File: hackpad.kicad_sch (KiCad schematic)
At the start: 1 part, among them U1 XIAO-RP2040-DIP

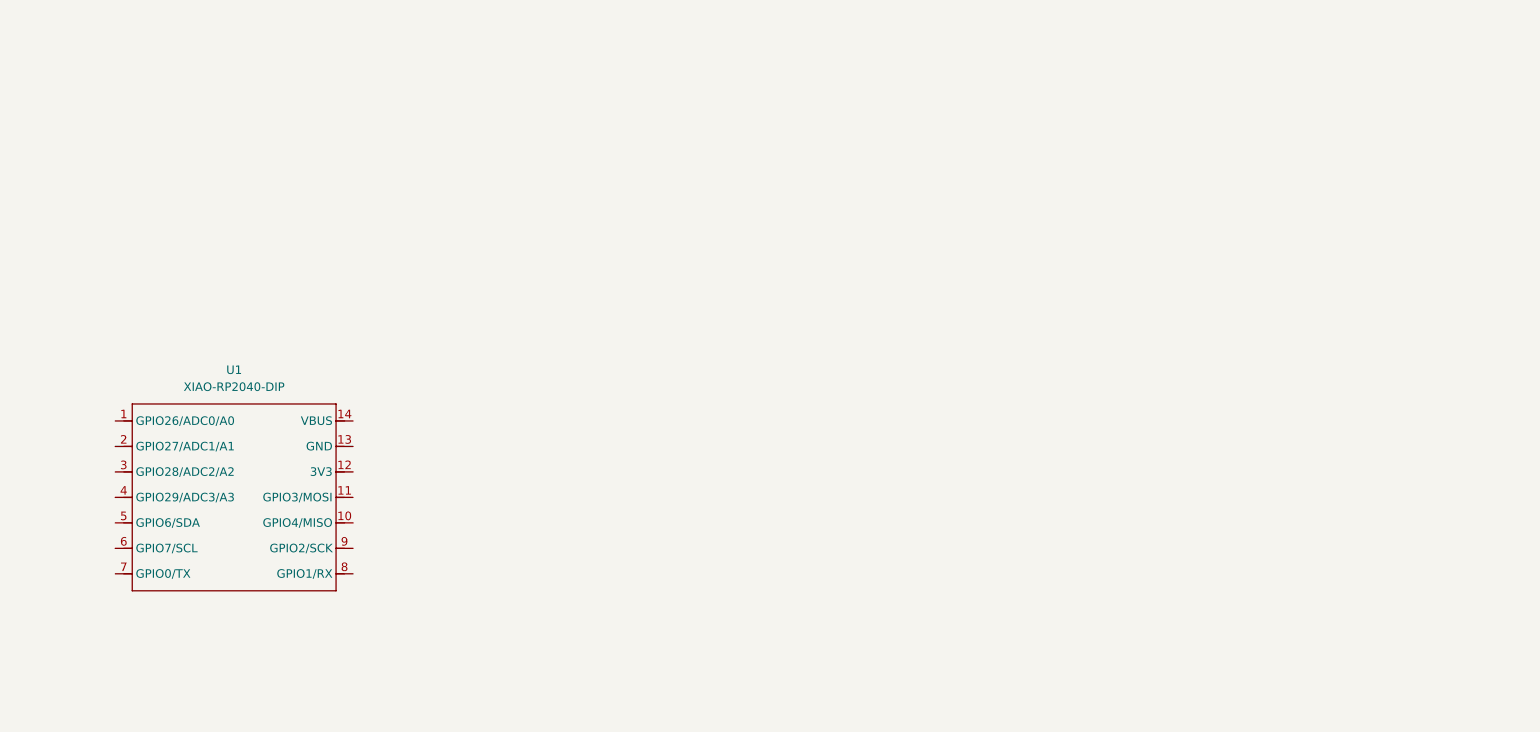
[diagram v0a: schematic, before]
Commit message: add keys, oled, neopixels to schematic
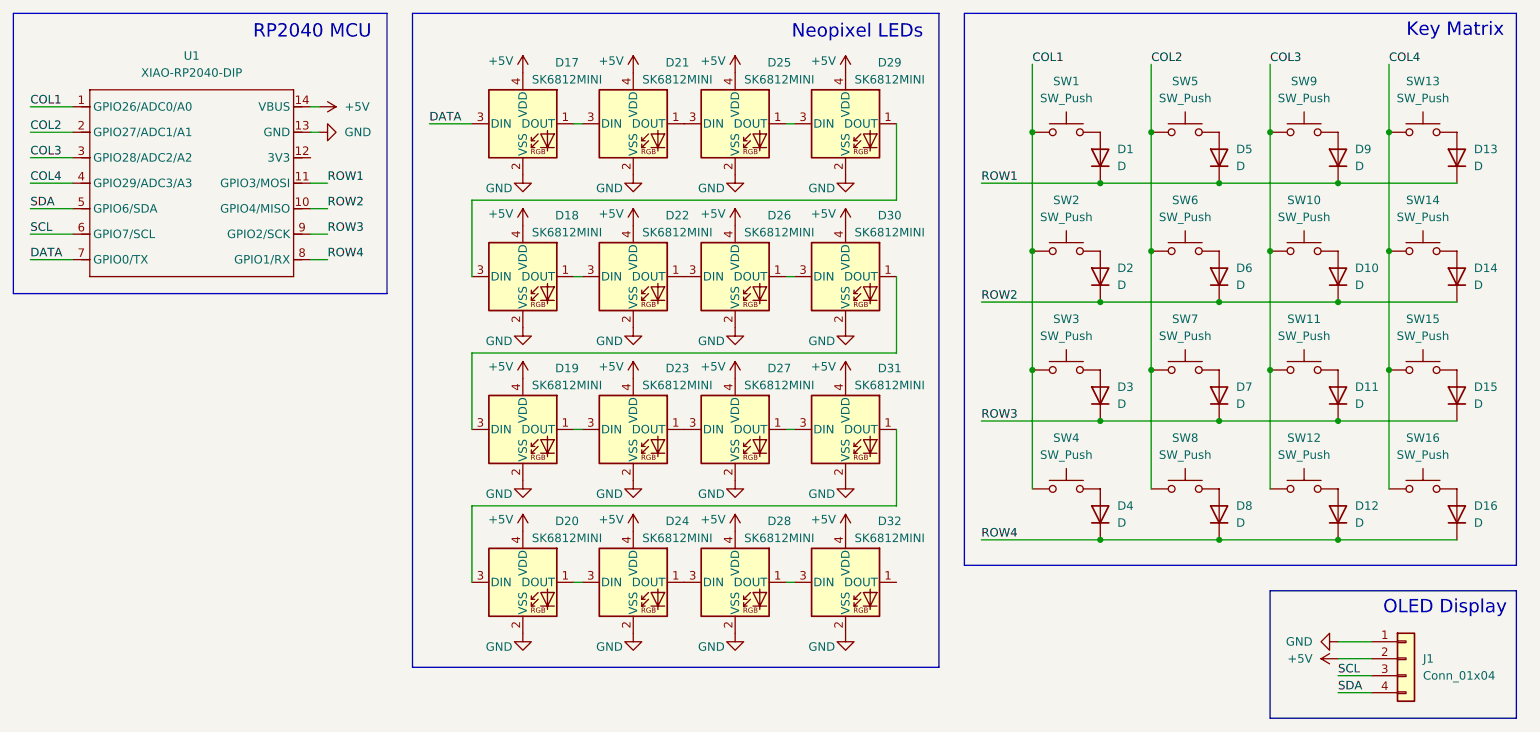
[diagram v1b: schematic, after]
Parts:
- added D1, D10, D11, D12, D13, D14, D15, D16, D2, D3, D4, D5, D6, D7, D8, D9: D, Diode_THT:D_DO-35_SOD27_P7.62mm_Horizontal, symbol Diode:1N4148
- added D17, D18, D19, D20, D21, D22, D23, D24, D25, D26, D27, D28, D29, D30, D31, D32: SK6812MINI, LED_SMD:LED_SK6812MINI_PLCC4_3.5x3.5mm_P1.75mm, symbol LED:SK6812MINI
- added J1: Conn_01x04, symbol Connector_Generic:Conn_01x04
- added SW1, SW10, SW11, SW12, SW13, SW14, SW15, SW16, SW2, SW3, SW4, SW5, SW6, SW7, SW8, SW9: SW_Push, symbol Switch:SW_Push
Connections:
- net COL1: now reaches U1.1 (GPIO26/ADC0/A0)
- net COL1: now also SW1.1, SW2.1, SW3.1, SW4.1
- net ROW2: now reaches U1.10 (GPIO4/MISO)
- net ROW2: now also D10.1 (K), D14.1 (K), D2.1 (K), D6.1 (K)
- net ROW1: now reaches U1.11 (GPIO3/MOSI)
- net ROW1: now also D1.1 (K), D13.1 (K), D5.1 (K), D9.1 (K)
- net GND: now reaches U1.13 (GND)
- net GND: now also D17.2 (VSS), D18.2 (VSS), D19.2 (VSS), D20.2 (VSS), D21.2 (VSS), D22.2 (VSS), D23.2 (VSS), D24.2 (VSS), D25.2 (VSS), D26.2 (VSS), D27.2 (VSS), D28.2 (VSS), D29.2 (VSS), D30.2 (VSS), D31.2 (VSS), D32.2 (VSS), J1.1 (Pin_1)
- net +5V: now reaches U1.14 (VBUS)
- net +5V: now also D17.4 (VDD), D18.4 (VDD), D19.4 (VDD), D20.4 (VDD), D21.4 (VDD), D22.4 (VDD), D23.4 (VDD), D24.4 (VDD), D25.4 (VDD), D26.4 (VDD), D27.4 (VDD), D28.4 (VDD), D29.4 (VDD), D30.4 (VDD), D31.4 (VDD), D32.4 (VDD), J1.2 (Pin_2)
- net COL2: now reaches U1.2 (GPIO27/ADC1/A1)
- net COL2: now also SW5.1, SW6.1, SW7.1, SW8.1
- net COL3: now reaches U1.3 (GPIO28/ADC2/A2)
- net COL3: now also SW10.1, SW11.1, SW12.1, SW9.1
- net COL4: now reaches U1.4 (GPIO29/ADC3/A3)
- net COL4: now also SW13.1, SW14.1, SW15.1, SW16.1
- net SDA: now reaches U1.5 (GPIO6/SDA)
- net SDA: now also J1.4 (Pin_4)
- net SCL: now reaches U1.6 (GPIO7/SCL)
- net SCL: now also J1.3 (Pin_3)
- net DATA: now reaches U1.7 (GPIO0/TX)
- net DATA: now also D17.3 (DIN)
- net ROW4: now reaches U1.8 (GPIO1/RX)
- net ROW4: now also D12.1 (K), D16.1 (K), D4.1 (K), D8.1 (K)
- net ROW3: now reaches U1.9 (GPIO2/SCK)
- net ROW3: now also D11.1 (K), D15.1 (K), D3.1 (K), D7.1 (K)
- new net: D7.2 (A), SW7.2
- new net: D21.1 (DOUT), D25.3 (DIN)
- new net: D17.1 (DOUT), D21.3 (DIN)
- new net: D10.2 (A), SW10.2
- new net: D4.2 (A), SW4.2
- new net: D11.2 (A), SW11.2
- new net: D1.2 (A), SW1.2
- new net: D14.2 (A), SW14.2
- new net: D2.2 (A), SW2.2
- new net: D27.1 (DOUT), D31.3 (DIN)
- new net: D23.1 (DOUT), D27.3 (DIN)
- new net: D20.1 (DOUT), D24.3 (DIN)
- new net: D20.3 (DIN), D31.1 (DOUT)
- new net: D13.2 (A), SW13.2
- new net: D25.1 (DOUT), D29.3 (DIN)
- new net: D24.1 (DOUT), D28.3 (DIN)
- new net: D19.1 (DOUT), D23.3 (DIN)
- new net: D19.3 (DIN), D30.1 (DOUT)
- new net: D15.2 (A), SW15.2
- new net: D8.2 (A), SW8.2
- new net: D18.1 (DOUT), D22.3 (DIN)
- new net: D18.3 (DIN), D29.1 (DOUT)
- new net: D28.1 (DOUT), D32.3 (DIN)
- new net: D5.2 (A), SW5.2
- new net: D6.2 (A), SW6.2
- new net: D9.2 (A), SW9.2
- new net: D26.1 (DOUT), D30.3 (DIN)
- new net: D3.2 (A), SW3.2
- new net: D12.2 (A), SW12.2
- new net: D22.1 (DOUT), D26.3 (DIN)
- new net: D16.2 (A), SW16.2
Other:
- note added: "Key Matrix"
- note added: "Neopixel LEDs"
- note added: "OLED Display"
- note added: "RP2040 MCU"
- moved on the sheet: U1

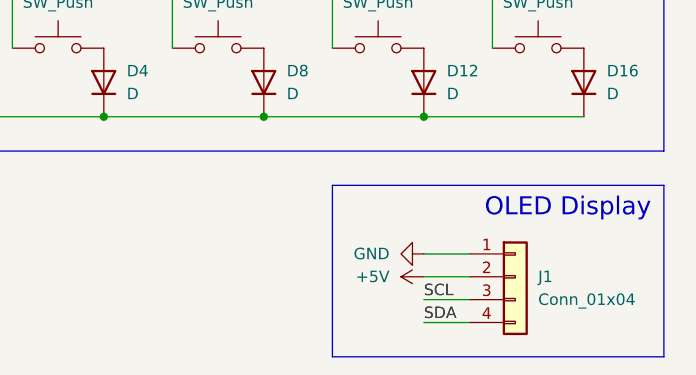
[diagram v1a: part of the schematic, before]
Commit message: add footprint submodules, first version of the pcb
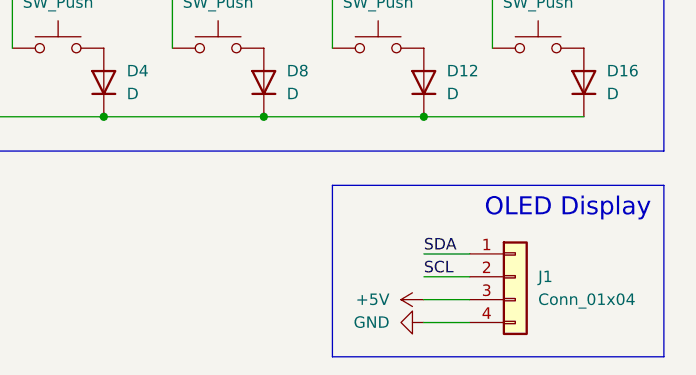
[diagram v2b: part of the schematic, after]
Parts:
- D17, D18, D19, D20, D21, D22, D23, D24, D25, D26, D27, D28, D29, D30, D31, D32: footprint LED_SMD:LED_SK6812MINI_PLCC4_3.5x3.5mm_P1.75mm -> Keebio-Parts:SK6812-MINI-E
- J1: footprint (none) -> KiCad-SSD1306-0.91-OLED-4pin-128x32:SSD1306-0.91-OLED-4pin-128x32
- SW1, SW10, SW11, SW12, SW13, SW14, SW15, SW16, SW2, SW3, SW4, SW5, SW6, SW7, SW8, SW9: footprint (none) -> Switch_Keyboard_Kailh:SW_Kailh_Choc_V2_1.00u
- U1: footprint Module:MOUDLE14P-XIAO-DIP-SMD -> OPL:XIAO-RP2040-DIP
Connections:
- net +5V: now also J1.3 (Pin_3); no longer J1.2 (Pin_2)
- net GND: now also J1.4 (Pin_4); no longer J1.1 (Pin_1)
- net SCL: now also J1.2 (Pin_2); no longer J1.3 (Pin_3)
- net SDA: now also J1.1 (Pin_1); no longer J1.4 (Pin_4)
